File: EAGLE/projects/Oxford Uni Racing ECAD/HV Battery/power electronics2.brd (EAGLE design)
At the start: 123.2 x 107.6 mm, 35 parts, among them IC1 4043N, IC2 4001N, IC3 LM555CN, IC4 4071N, K1 T9AS1D12-48=T9A, K2 T9AS5D12-12=T9A, K4 T9AS1D12-48=T9A, K5 T9AS1D12-48=T9A, Q1 BSS92, Q2 BSS92

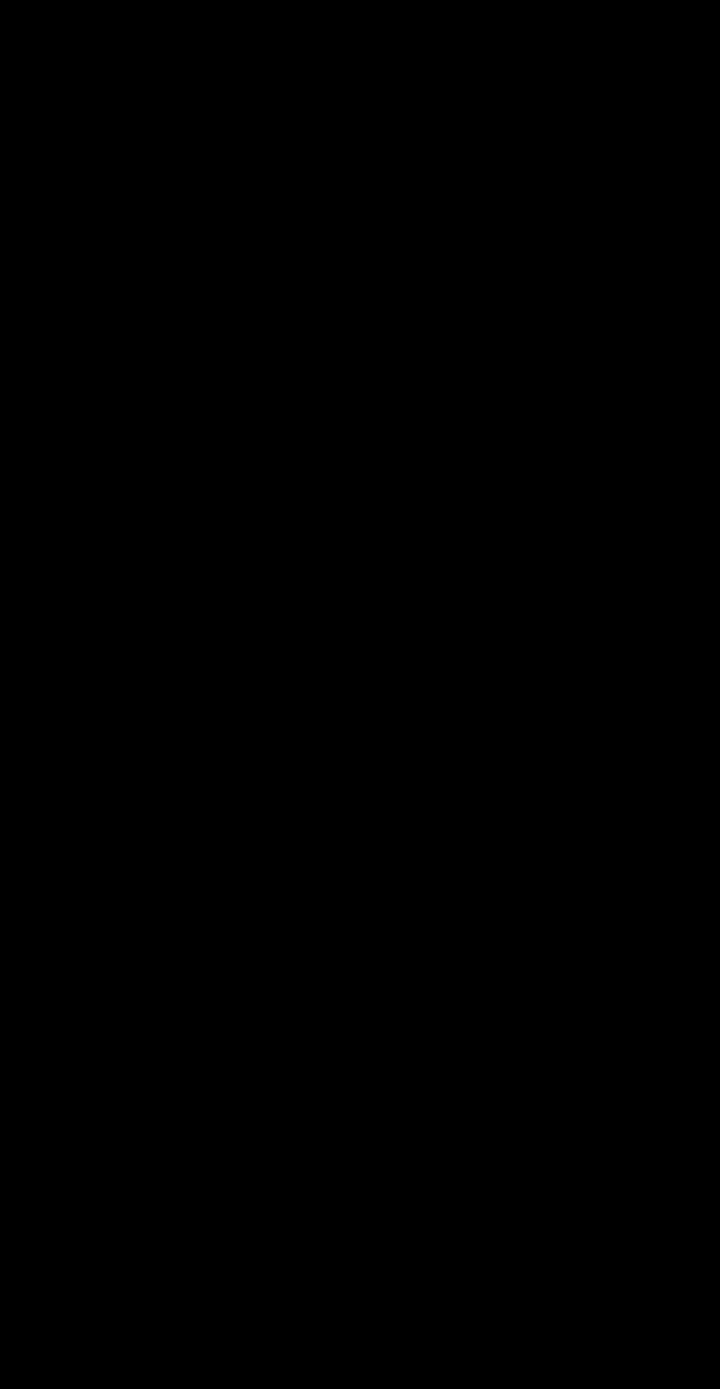
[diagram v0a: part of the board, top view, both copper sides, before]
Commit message: Added positive edge detection for ams relays and leds
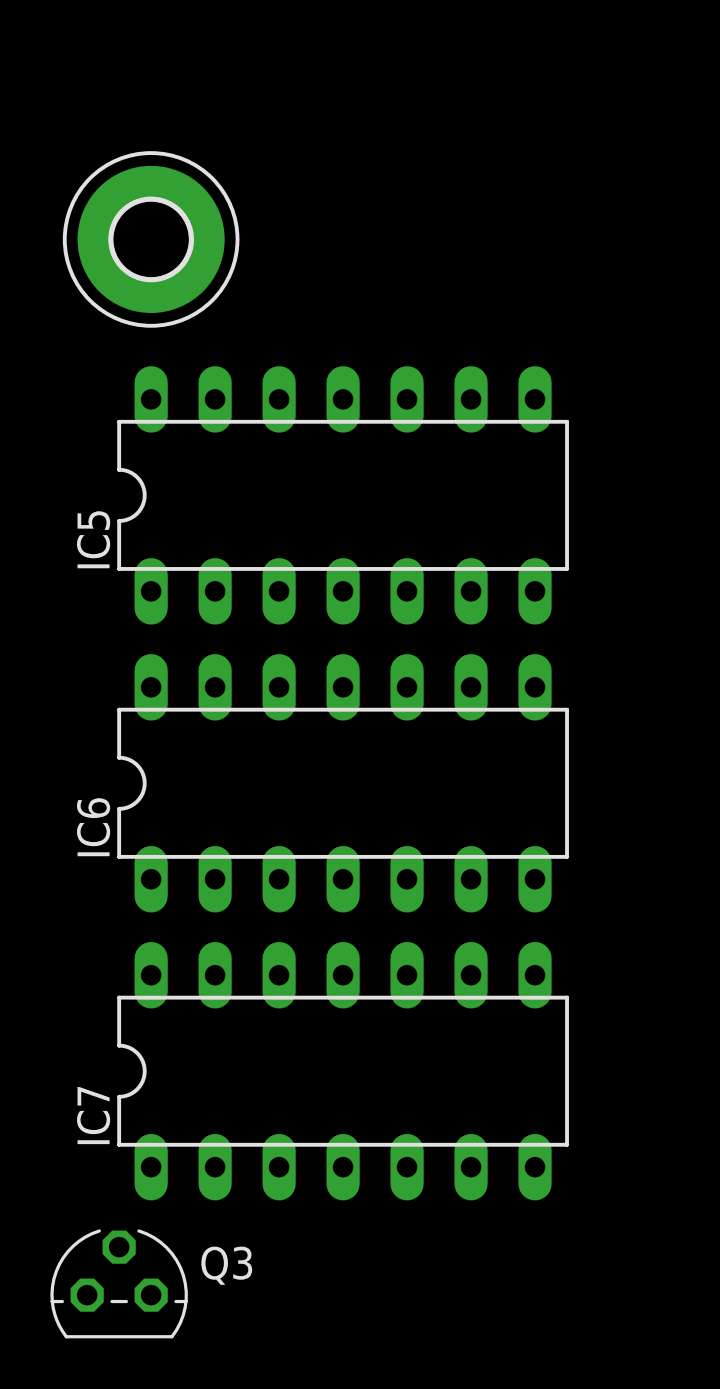
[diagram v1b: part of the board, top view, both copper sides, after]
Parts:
- added GND: MOUNT-PAD-ROUND3.0, holes:3,0-PAD
- added IC5: 4081N, 40xx:DIL14
- added IC6, IC7: 4011N, 40xx:DIL14
- added Q3: BSS92, transistor-fet:TO92
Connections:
- new net AMS_LED_OUT: MISC_I/O.5, Q3.2
- new net N$23: IC1.6, IC5.4
- new net N$24: IC6.3, IC6.5, IC6.6
- new net N$25: IC6.4, IC6.8, IC6.9
- new net N$26: IC5.6, IC6.10
- new net N$27: IC1.12, IC5.3
- new net N$28: IC5.2, IC7.4
- new net N$29: IC1.10, IC1.9, Q3.1
- new net N$30: IC7.3, IC7.5, IC7.6
- new net N$32: IC6.11, IC7.1, IC7.2
- new net VDD: IC5.14, IC6.14, IC7.14
- new net VSS: IC5.7, IC6.7, IC7.7
- net +12V: now also Q3.3
- net CHG_SAFE: now also IC5.1, IC6.12, IC6.13
- net DISCHARGE_ENABLE: now also IC5.5, IC6.1, IC6.2
- net GND: now also GND.B3,0
- net N$20: now also IC1.11, IC1.7
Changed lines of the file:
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@@
 <attribute name="VALUE" x="-3.175" y="-36.83" size="1.27" layer="27" ratio="10"/>
+</element>
+<element name="GND" library="holes" library_urn="urn:adsk.eagle:library:237" package="3,0-PAD" package3d_urn="urn:adsk.eagle:package:14280/1" value="MOUNT-PAD-ROUND3.0" x="-13.97" y="-49.53" smashed="yes"/>
+<element name="IC5" library="40xx" library_urn="urn:adsk.eagle:library:80" package="DIL14" package3d_urn="urn:adsk.eagle:package:16407/2" value="4081N" x="-6.35" y="-59.69" smashed="yes">
+<attribute name="NAME" x="-15.621" y="-62.738" size="1.27" layer="25" ratio="10" rot="R90"/>
+<attribute name="VALUE" x="-13.081" y="-60.325" size="1.27" layer="27" ratio="10"/>
+</element>
+<element name="IC6" library="40xx" library_urn="urn:adsk.eagle:library:80" package="DIL14" package3d_urn="urn:adsk.eagle:package:16407/2" value="4011N" x="-6.35" y="-71.12" smashed="yes">
+<attribute name="NAME" x="-15.621" y="-74.168" size="1.27" layer="25" ratio="10" rot="R90"/>
+<attribute name="VALUE" x="-13.081" y="-71.755" size="1.27" layer="27" ratio="10"/>
+</element>
+<element name="IC7" library="40xx" library_urn="urn:adsk.eagle:library:80" package="DIL14" package3d_urn="urn:adsk.eagle:package:16407/2" value="4011N" x="-6.35" y="-82.55" smashed="yes">
+<attribute name="NAME" x="-15.621" y="-85.598" size="1.27" layer="25" ratio="10" rot="R90"/>
+<attribute name="VALUE" x="-13.081" y="-83.185" size="1.27" layer="27" ratio="10"/>
+</element>
+<element name="Q3" library="transistor-fet" library_urn="urn:adsk.eagle:library:396" package="TO92" package3d_urn="urn:adsk.eagle:package:28523/2" value="BSS92" x="-15.24" y="-91.44" smashed="yes">
+<attribute name="NAME" x="-12.065" y="-90.805" size="1.27" layer="25" ratio="10"/>
+<attribute name="VALUE" x="-12.065" y="-92.71" size="1.27" layer="27" ratio="10"/>
 </element>
 </elements>
@@
 <contactref element="IC4" pad="7"/>
 <contactref element="MISC_I/O" pad="4"/>
+<contactref element="GND" pad="B3,0"/>
 <wire x1="106.68" y1="60.96" x2="113.03" y2="64.77" width="0" layer="19" extent="1-1"/>
 <wire x1="107.95" y1="38.1" x2="106.68" y2="60.96" width="0" layer="19" extent="1-1"/>
@@
 <wire x1="-3.81" y1="-13.97" x2="-3.81" y2="-8.89" width="0" layer="19" extent="1-1"/>
 <wire x1="10.16" y1="-30.48" x2="-3.81" y2="-13.97" width="0" layer="19" extent="1-1"/>
+<wire x1="-13.97" y1="-49.53" x2="10.16" y2="-30.48" width="0" layer="19" extent="1-1"/>
 </signal>
 <signal name="N$1">
@@
 <contactref element="K5" pad="2"/>
 <contactref element="D6" pad="A"/>
+<contactref element="IC5" pad="1"/>
+<contactref element="IC6" pad="12"/>
+<contactref element="IC6" pad="13"/>
 <wire x1="41.91" y1="44.45" x2="113.03" y2="49.53" width="0" layer="19" extent="1-1"/>
 <wire x1="30.48" y1="49.53" x2="41.91" y2="44.45" width="0" layer="19" extent="1-1"/>
+<wire x1="-13.97" y1="-63.5" x2="30.48" y2="49.53" width="0" layer="19" extent="1-1"/>
+<wire x1="-11.43" y1="-67.31" x2="-13.97" y2="-63.5" width="0" layer="19" extent="1-1"/>
+<wire x1="-8.89" y1="-67.31" x2="-11.43" y2="-67.31" width="0" layer="19" extent="1-1"/>
 </signal>
 <signal name="DISCHARGE_ENABLE">
@@
 <contactref element="K4" pad="1"/>
 <contactref element="D7" pad="A"/>
+<contactref element="IC6" pad="1"/>
+<contactref element="IC6" pad="2"/>
+<contactref element="IC5" pad="5"/>
+<wire x1="43.18" y1="91.44" x2="110.49" y2="49.53" width="0" layer="19" extent="1-1"/>
 <wire x1="30.48" y1="92.71" x2="43.18" y2="91.44" width="0" layer="19" extent="1-1"/>
-<wire x1="110.49" y1="49.53" x2="43.18" y2="91.44" width="0" layer="19" extent="1-1"/>
+<wire x1="-3.81" y1="-63.5" x2="30.48" y2="92.71" width="0" layer="19" extent="1-1"/>
+<wire x1="-11.43" y1="-74.93" x2="-3.81" y2="-63.5" width="0" layer="19" extent="1-1"/>
+<wire x1="-13.97" y1="-74.93" x2="-11.43" y2="-74.93" width="0" layer="19" extent="1-1"/>
 </signal>
 <signal name="N$4">
@@
 <contactref element="IC3" pad="8"/>
 <contactref element="R4" pad="2"/>
-<contactref element="IC3" pad="4"/>
 <contactref element="IC3" pad="2"/>
 <contactref element="IC4" pad="14"/>
 <contactref element="Q1" pad="3"/>
 <contactref element="Q2" pad="3"/>
+<contactref element="IC3" pad="4"/>
+<contactref element="Q3" pad="3"/>
 <wire x1="105.41" y1="35.56" x2="113.03" y2="62.23" width="0" layer="19" extent="1-1"/>
 <wire x1="73.66" y1="27.94" x2="105.41" y2="35.56" width="0" layer="19" extent="1-1"/>
@@
 <wire x1="-5.08" y1="-22.86" x2="-7.62" y2="-19.05" width="0" layer="19" extent="1-1"/>
 <wire x1="-7.62" y1="-35.56" x2="-5.08" y2="-22.86" width="0" layer="19" extent="1-1"/>
+<wire x1="-16.51" y1="-91.44" x2="-7.62" y2="-35.56" width="0" layer="19" extent="1-1"/>
 </signal>
 <signal name="N$5">
@@
 </signal>
 <signal name="N$20">
+<contactref element="IC1" pad="3"/>
 <contactref element="IC3" pad="3"/>
-<contactref element="IC1" pad="3"/>
+<contactref element="IC1" pad="7"/>
+<contactref element="IC1" pad="11"/>
+<wire x1="57.15" y1="19.05" x2="54.61" y2="26.67" width="0" layer="19" extent="1-1"/>
+<wire x1="46.99" y1="19.05" x2="57.15" y2="19.05" width="0" layer="19" extent="1-1"/>
 <wire x1="-8.89" y1="5.08" x2="46.99" y2="19.05" width="0" layer="19" extent="1-1"/>
 </signal>
@@
 <wire x1="-6.35" y1="-33.655" x2="30.48" y2="27.94" width="0" layer="19" extent="1-1"/>
 </signal>
+<signal name="VSS">
+<contactref element="IC5" pad="7"/>
+<contactref element="IC6" pad="7"/>
+<contactref element="IC7" pad="7"/>
+<wire x1="1.27" y1="-74.93" x2="1.27" y2="-86.36" width="0" layer="19" extent="1-1"/>
+<wire x1="1.27" y1="-63.5" x2="1.27" y2="-74.93" width="0" layer="19" extent="1-1"/>
+</signal>
+<signal name="VDD">
+<contactref element="IC5" pad="14"/>
+<contactref element="IC6" pad="14"/>
+<contactref element="IC7" pad="14"/>
+<wire x1="-13.97" y1="-67.31" x2="-13.97" y2="-78.74" width="0" layer="19" extent="1-1"/>
+<wire x1="-13.97" y1="-55.88" x2="-13.97" y2="-67.31" width="0" layer="19" extent="1-1"/>
+</signal>
+<signal name="N$24">
+<contactref element="IC6" pad="5"/>
+<contactref element="IC6" pad="6"/>
+<contactref element="IC6" pad="3"/>
+<wire x1="-3.81" y1="-74.93" x2="-8.89" y2="-74.93" width="0" layer="19" extent="1-1"/>
+<wire x1="-1.27" y1="-74.93" x2="-3.81" y2="-74.93" width="0" layer="19" extent="1-1"/>
+</signal>
+<signal name="N$25">
+<contactref element="IC6" pad="8"/>
+<contactref element="IC6" pad="9"/>
+<contactref element="IC6" pad="4"/>
+<wire x1="-1.27" y1="-67.31" x2="-6.35" y2="-74.93" width="0" layer="19" extent="1-1"/>
+<wire x1="1.27" y1="-67.31" x2="-1.27" y2="-67.31" width="0" layer="19" extent="1-1"/>
+</signal>
+<signal name="N$26">
+<contactref element="IC6" pad="10"/>
+<contactref element="IC5" pad="6"/>
+<wire x1="-1.27" y1="-63.5" x2="-3.81" y2="-67.31" width="0" layer="19" extent="1-1"/>
+</signal>
+<signal name="N$28">
+<contactref element="IC7" pad="4"/>
+<contactref element="IC5" pad="2"/>
+<wire x1="-11.43" y1="-63.5" x2="-6.35" y2="-86.36" width="0" layer="19" extent="1-1"/>
+</signal>
+<signal name="N$30">
+<contactref element="IC7" pad="5"/>
+<contactref element="IC7" pad="6"/>
+<contactref element="IC7" pad="3"/>
+<wire x1="-3.81" y1="-86.36" x2="-8.89" y2="-86.36" width="0" layer="19" extent="1-1"/>
+<wire x1="-1.27" y1="-86.36" x2="-3.81" y2="-86.36" width="0" layer="19" extent="1-1"/>
+</signal>
+<signal name="N$32">
+<contactref element="IC7" pad="1"/>
+<contactref element="IC7" pad="2"/>
+<contactref element="IC6" pad="11"/>
+<wire x1="-11.43" y1="-86.36" x2="-13.97" y2="-86.36" width="0" layer="19" extent="1-1"/>
+<wire x1="-6.35" y1="-67.31" x2="-11.43" y2="-86.36" width="0" layer="19" extent="1-1"/>
+</signal>
+<signal name="N$23">
+<contactref element="IC5" pad="4"/>
+<contactref element="IC1" pad="6"/>
+<wire x1="-6.35" y1="-63.5" x2="54.61" y2="19.05" width="0" layer="19" extent="1-1"/>
+</signal>
+<signal name="N$27">
+<contactref element="IC5" pad="3"/>
+<contactref element="IC1" pad="12"/>
+<wire x1="-8.89" y1="-63.5" x2="52.07" y2="26.67" width="0" layer="19" extent="1-1"/>
+</signal>
+<signal name="N$29">
+<contactref element="IC1" pad="9"/>
+<contactref element="IC1" pad="10"/>
+<contactref element="Q3" pad="1"/>
+<wire x1="57.15" y1="26.67" x2="-13.97" y2="-91.44" width="0" layer="19" extent="1-1"/>
+<wire x1="59.69" y1="26.67" x2="57.15" y2="26.67" width="0" layer="19" extent="1-1"/>
+</signal>
+<signal name="AMS_LED_OUT">
+<contactref element="Q3" pad="2"/>
+<contactref element="MISC_I/O" pad="5"/>
+<wire x1="-15.24" y1="-89.535" x2="110.49" y2="35.56" width="0" layer="19" extent="1-1"/>
+</signal>
 </signals>
